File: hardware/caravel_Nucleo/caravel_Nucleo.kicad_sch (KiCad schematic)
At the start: 6 parts, among them J10 Conn_01x09_Female, J3 Conn_01x02_Male, J5 Conn_01x02_Male, T1 Logo, T2 Logo, U11 NUCLEO144-F429ZI

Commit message: [in review] update caravel board Nucleo-144 hat
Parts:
- added C1: 0.01uf - CC0805JRX7R9BB103, Capacitor_SMD:C_0805_2012Metric, symbol Device:C
- added C10, C13, C18, C20, C21: 1uf - CC0805KKX5R8BB105, Capacitor_SMD:C_0805_2012Metric, symbol Device:C
- added C11, C14, C19: 0.01uf - CC0805KRX7R9BB103, Capacitor_SMD:C_0805_2012Metric, symbol Device:C
- added C12, C15: 10uf - CC0805KKX5R8BB106, Capacitor_SMD:C_0805_2012Metric, symbol Device:C
- added C16, C17, C2, C3, C4, C5, C6, C7, C8, C9: 0.1uf - CC0805KRX7R9BB104, Capacitor_SMD:C_0805_2012Metric, symbol Device:C
- added D1, D2, D3, D4: LED - 17-215SURC/S530-A2/TR8, LED_SMD:LED_1206_3216Metric, symbol Device:LED
- added J1: USB_B_Micro - 10118193-0001LF, strive_foot_prints:FCI_10118193-0001LF, symbol Connector:USB_B_Micro
- added J11, J8, J9: Conn_01x03, Connector_PinHeader_2.54mm:PinHeader_1x03_P2.54mm_Vertical, symbol Connector_Generic:Conn_01x03
- added J2: Conn_01x02_Female, Connector_PinHeader_2.54mm:PinHeader_1x02_P2.54mm_Vertical, symbol Connector:Conn_01x02_Female
- added J4: Conn_01x04_Female, Connector_PinHeader_2.54mm:PinHeader_1x04_P2.54mm_Vertical, symbol Connector:Conn_01x04_Female
- added J6: Conn_01x02_Male, Connector_PinHeader_2.54mm:PinHeader_1x02_P2.54mm_Vertical, symbol Connector:Conn_01x02_Male
- added J7: Conn_01x06_Female, Connector_PinHeader_2.54mm:PinHeader_1x06_P2.54mm_Vertical, symbol Connector:Conn_01x06_Female
- added R1, R10, R11, R12, R7, R8, R9: 10k - RC0805FR-0710KL, Resistor_SMD:R_0805_2012Metric, symbol Device:R
- added R13, R14: 82 - 0805W8F820JT5E, Resistor_SMD:R_0805_2012Metric, symbol Device:R
- added R15, R16, R17, R18, R27, R5, R6: 10k, Resistor_SMD:R_0805_2012Metric, symbol Device:R
- added R19: 360 1% - 0805W8F1202T5E, Resistor_SMD:R_0805_2012Metric, symbol Device:R
- added R2: 12K 1% - 0805W8F1202T5E, Resistor_SMD:R_0805_2012Metric, symbol Device:R
- added R20, R23: 4.99K 1% - 0805W8F1202T5E, Resistor_SMD:R_0805_2012Metric, symbol Device:R
- added R21: 499 1% - 0805W8F1202T5E, Resistor_SMD:R_0805_2012Metric, symbol Device:R
- added R22: 4.22K 1% - 0805W8F1202T5E, Resistor_SMD:R_0805_2012Metric, symbol Device:R
- added R24: 4.02K 1% - 0805W8F1202T5E, Resistor_SMD:R_0805_2012Metric, symbol Device:R
- added R25, R26: 4.7K 1% - 0805W8F1202T5E, Resistor_SMD:R_0805_2012Metric, symbol Device:R
- added R3, R4: 150 - 0805W8J0151T5E, Resistor_SMD:R_0805_2012Metric, symbol Device:R
- added SW1: SW_Push - SKQGADE010, strive_foot_prints:SW4-SMD-5.2X5.2X1.5MM, symbol Switch:SW_Push
- added TP1, TP2: TestPoint, TestPoint:TestPoint_Bridge_Pitch2.54mm_Drill1.0mm, symbol Connector:TestPoint
- added U1: FT232H, Package_DFN_QFN:QFN-48-1EP_8x8mm_P0.5mm_EP6.2x6.2mm, symbol Interface_USB:FT232H
- added U10: MCP4661, Caravel_Board:QFN-16-1EP_4x4mm_P0.65mm_EP2.5x2.5mm, symbol Caravel_board:MCP4661
- added U2, U3: SN74LVC1G125DCKR, SOT65P210X110-5N, symbol Caravel_board:SN74LVC1G125DCKR
- added U4: MCP1319MT-29LE-OT, Caravel_Board:PoR_5_SOT23, symbol Caravel_board:MCP1319MT-29LE-OT
- added U5, U6: TAR5SxxU_SOT353F, Caravel_Board:SOT-353F, symbol Caravel_board:TAR5SxxU_SOT353F
- added U7: W25Q32FVSS, strive_foot_prints:SOIC127P790X216-8N, symbol Caravel_board:W25Q32FVSS
- added U8: caravel_breakout, Caravel_Board:caravel_breakout_flexy, symbol Caravel_board:caravel_breakout_v2
- added U9: MIC2211-AAYML-TR, Caravel_Board:10-pin_MLF_P0.5, symbol Caravel_board:MIC2211-AAYML-TR
- added X1: DSC6001_10MHZ, strive_foot_prints:DSC6001JE1A-010.0000, symbol Oscillator:XO91
- added Y1: CSTNE12M0GH5L000R0, strive_foot_prints:CSTNE12M0GH5L000R0, symbol Device:Crystal_GND2
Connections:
- net vccd1 is gone; now on net +1V8: J3.2 (Pin_2)
- net vddio is gone; now on net +3V3: J5.2 (Pin_2)
- net +1V8: now also J8.2 (Pin_2), U8.43 (vccd1), U8.50 (vccd), U8.6 (vccd)
- net +3V3: now also C16.2, C17.1, C4.2, C5.2, C6.2, C7.2, C8.2, C9.2, J4.4 (Pin_4), J9.2 (Pin_2), R1.2, R10.2, R11.2, R12.2, R13.1, R14.1, R3.2, R4.2, R5.1, R6.1, R7.2, R8.2, R9.2, U1.12 (VCCIO), U1.24 (VCCIO), U1.3 (VPHY), U1.39 (VCCD), U1.40 (VREGIN), U1.46 (VCCIO), U1.8 (VPLL), U2.5 (VCC), U3.5 (VCC), U4.5 (VDD), U7.8 (VCC), U8.45 (vdda), U8.55 (vddio), U8.7 (vddio), X1.4 (V+)
- net +5V: now also C10.2, C13.2, C18.2, J1.1 (VBUS), R15.2, R16.2, R17.2, R18.2, R25.1, R26.1, R27.2, U10.14 (VDD), U5.5 (VIN), U6.5 (VIN), U9.1 (VIN)
- net Caravel_CSB: now also J7.1 (Pin_1), R7.1, U7.1 (~{CS}), U8.51 (Caravel_CSB)
- net Caravel_D0: now also J7.4 (Pin_4), R10.1, U7.5 (SI(D0)), U8.49 (Caravel_D0)
- net Caravel_D1: now also J7.2 (Pin_2), R8.1, U7.2 (SO(D1)), U8.48 (Caravel_D1)
- net Caravel_SCK: now also J7.5 (Pin_5), R11.1, U7.6 (SCK), U8.46 (Caravel_SCK)
- net GND: now also C1.1, C10.1, C11.2, C12.1, C13.1, C14.2, C15.1, C16.1, C17.2, C18.1, C19.2, C2.1, C20.2, C21.2, C3.1, C4.1, C5.1, C6.1, C7.1, C8.1, C9.1, D4.1 (K), J1.5 (GND), J2.1 (Pin_1), J4.1 (Pin_1), J6.2 (Pin_2), R2.1, R20.1, R24.1, SW1.2, TP1.1, TP2.1, U1.10 (GND), U1.11 (GND), U1.22 (GND), U1.23 (GND), U1.35 (GND), U1.36 (GND), U1.4 (AGND), U1.41 (AGND), U1.42 (TEST), U1.47 (GND), U1.48 (GND), U1.9 (AGND), U10.1 (HVC/A0), U10.10 (P0B), U10.12 (A2), U10.13 (A1), U10.4 (VSS), U10.5 (P1B), U2.3 (GND), U3.3 (GND), U4.2 (VSS), U5.2 (GND), U6.2 (GND), U7.4 (GND), U8.5 (GND), U8.8 (GND), U9.6 (GND), X1.2 (GND), Y1.2
- net I2C2_SCL: now also R25.2, U10.2 (SCL)
- net I2C2_SDA: now also R26.2, U10.3 (SDA)
- net SPI5_CS: now also U1.16 (ADBUS3), U8.39 (mprj_io[3]_CSB)
- net SPI5_MISO: now also U1.14 (ADBUS1), U2.4 (Y), U8.40 (mprj_io[2]_SDI)
- net SPI5_MOSI: now also U1.15 (ADBUS2), U8.41 (mprj_io[1]_SDO)
- net SPI5_SCK: now also U1.13 (ADBUS0), U3.2 (A), U8.38 (mprj_io[4]_SCK)
- net TIM3_CH2: now also J11.1 (Pin_1); no longer J10.9 (Pin_9)
- net gpio: now also D3.1 (K), U8.47 (gpio)
- net mprj_io[0]: now also U8.42 (mprj_io[0])
- net mprj_io[10]: now also U8.32 (mprj_io[10])
- net mprj_io[11]: now also U8.31 (mprj_io[11])
- net mprj_io[12]: now also U8.30 (mprj_io[12])
- net mprj_io[13]: now also U8.29 (mprj_io[13])
- net mprj_io[14]: now also U8.28 (mprj_io[14])
- net mprj_io[15]: now also U8.27 (mprj_io[15])
- net mprj_io[16]: now also U8.26 (mprj_io[16])
- net mprj_io[17]: now also U8.25 (mprj_io[17])
- net mprj_io[18]: now also U8.24 (mprj_io[18])
- net mprj_io[19]: now also U8.23 (mprj_io[19])
- net mprj_io[20]: now also U8.22 (mprj_io[20])
- net mprj_io[21]: now also U8.21 (mprj_io[21])
- net mprj_io[22]: now also U8.20 (mprj_io[22])
- net mprj_io[23]: now also U8.19 (mprj_io[23])
- net mprj_io[24]: now also U8.18 (mprj_io[24])
- net mprj_io[25]: now also U8.17 (mprj_io[25])
- net mprj_io[26]: now also U8.16 (mprj_io[26])
- net mprj_io[27]: now also U8.15 (mprj_io[27])
- net mprj_io[28]: now also U8.14 (mprj_io[28])
- net mprj_io[29]: now also U8.13 (mprj_io[29])
- net mprj_io[30]: now also U8.12 (mprj_io[30])
- net mprj_io[31]: now also U8.11 (mprj_io[31])
- net mprj_io[32]: now also U8.10 (mprj_io[32])
- net mprj_io[33]: now also U8.9 (mprj_io[33])
- net mprj_io[34]: now also U8.4 (mprj_io[34])
- net mprj_io[35]: now also U8.3 (mprj_io[35])
- net mprj_io[36]: now also U8.2 (mprj_io[36])
- net mprj_io[37]: now also U8.1 (mprj_io[37])
- net mprj_io[7]: now also U8.35 (mprj_io[7])
- net mprj_io[8]: now also U8.34 (mprj_io[8])
- net mprj_io[9]: now also U8.33 (mprj_io[9])
- net vccd2: now also U8.56 (vccd2)
- net vdda1: now also U8.44 (vdda1)
- net vdda2: now also U8.54 (vdda2)
- net ~{RST}: now also U4.1 (~{RST}), U8.53 (~{RST})
- net UART8_RX: now reaches U11.136 (PE0)
- net UART8_RX: now also J4.3 (Pin_3), U2.2 (A), U8.36 (mprj_io[6]_ser_tx)
- net PH0: now reaches U11.29 (PH0)
- net PH0: now also J11.3 (Pin_3)
- net UART8_TX: now reaches U11.61 (PE1)
- net UART8_TX: now also J4.2 (Pin_2), U3.4 (Y), U8.37 (mprj_io[5]_ser_rx)
- net UART3_RX: no longer names the net of U11.2 (PC11)
- net UART3_TX: no longer names the net of U11.1 (PC10)
- new net: R2.2, U1.5 (REF)
- new net: R16.1, U6.1 (Control)
- new net: C14.1, U6.3 (Noise)
- new net: R27.1, U10.11 (~{WP})
- new net: R23.1, U10.6 (P1W)
- new net: R21.1, U10.9 (P0W)
- new net: J6.1 (Pin_1), X1.1 (EN)
- new net: R18.1, U9.2 (EN1)
- new net: C11.1, U5.3 (Noise)
- new net: R19.1, R20.2, R21.2, U9.5 (ADJ1)
- new net: D4.2 (A), R14.2
- new net: C19.1, U9.4 (BYP)
- new net: R22.1, R23.2, R24.2, U9.7 (ADJ2)
- new net: U1.1 (XCSI), Y1.1
- new net: U1.2 (XCSO), Y1.3
- new net: D2.1 (K), U1.26 (ACBUS2)
- new net: D1.1 (K), U1.27 (ACBUS3)
- new net: C1.2, R1.1, U1.34 (~{RESET})
- new net: C3.2, U1.37 (VCCA)
- new net: C2.2, U1.38 (VCCCORE)
- new net: D2.2 (A), R4.1
- new net: D3.2 (A), R13.2
- new net: D1.2 (A), R3.1
- new net: R15.1, U5.1 (Control)
- new net: R17.1, U9.3 (EN2)
- new net FTDI_D+: J1.3 (D+), U1.7 (DP)
- new net FTDI_D-: J1.2 (D-), U1.6 (DM)
- new net UART_EN: J2.2 (Pin_2), R5.2, R6.2, U1.21 (ACBUS0), U2.1 (~{OE}), U3.1 (~{OE})
- new net V1.8: C15.2, J8.1 (Pin_1), U6.4 (VOUT)
- new net V3.3: C12.2, J9.1 (Pin_1), U5.4 (VOUT)
- new net VOUT1: C20.1, J9.3 (Pin_3), R19.2, U9.10 (VOUT1)
- new net VOUT2: C21.1, J8.3 (Pin_3), R22.2, U9.9 (VOUT2)
- new net xclk: J10.9 (Pin_9), J11.2 (Pin_2), U8.52 (xclk), X1.3 (OUT)
- new net ~{MEM_HOLD}: J7.6 (Pin_6), R12.1, U7.7 (~{HOLD}(D3))
- new net ~{MEM_WP}: J7.3 (Pin_3), R9.1, U7.3 (~{WP}(D2))
- new net ~{MR}: SW1.1, U4.4 (~{MR})
- no-connect marks 7 -> 24
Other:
- removed sheet Caravel Board
- note added: "Buffers to enable FTDI UART interface"
- note added: "Dynamic Power Supplies"
- note added: "FTDI Module"
- note added: "FTDI interface with HKSPI"
- note added: "Flash memory"
- note added: "Flash memory interface with Caravel"
- note added: "LEDs"
- note added: "MEMS Oscillator"
- note added: "Memory testing"
- note added: "Power on Reset"
- note added: "Serial Display"
- note added: "USB Module"
- note added: "Voltage Regulator"
- moved on the sheet: J10, J3, J5, U11

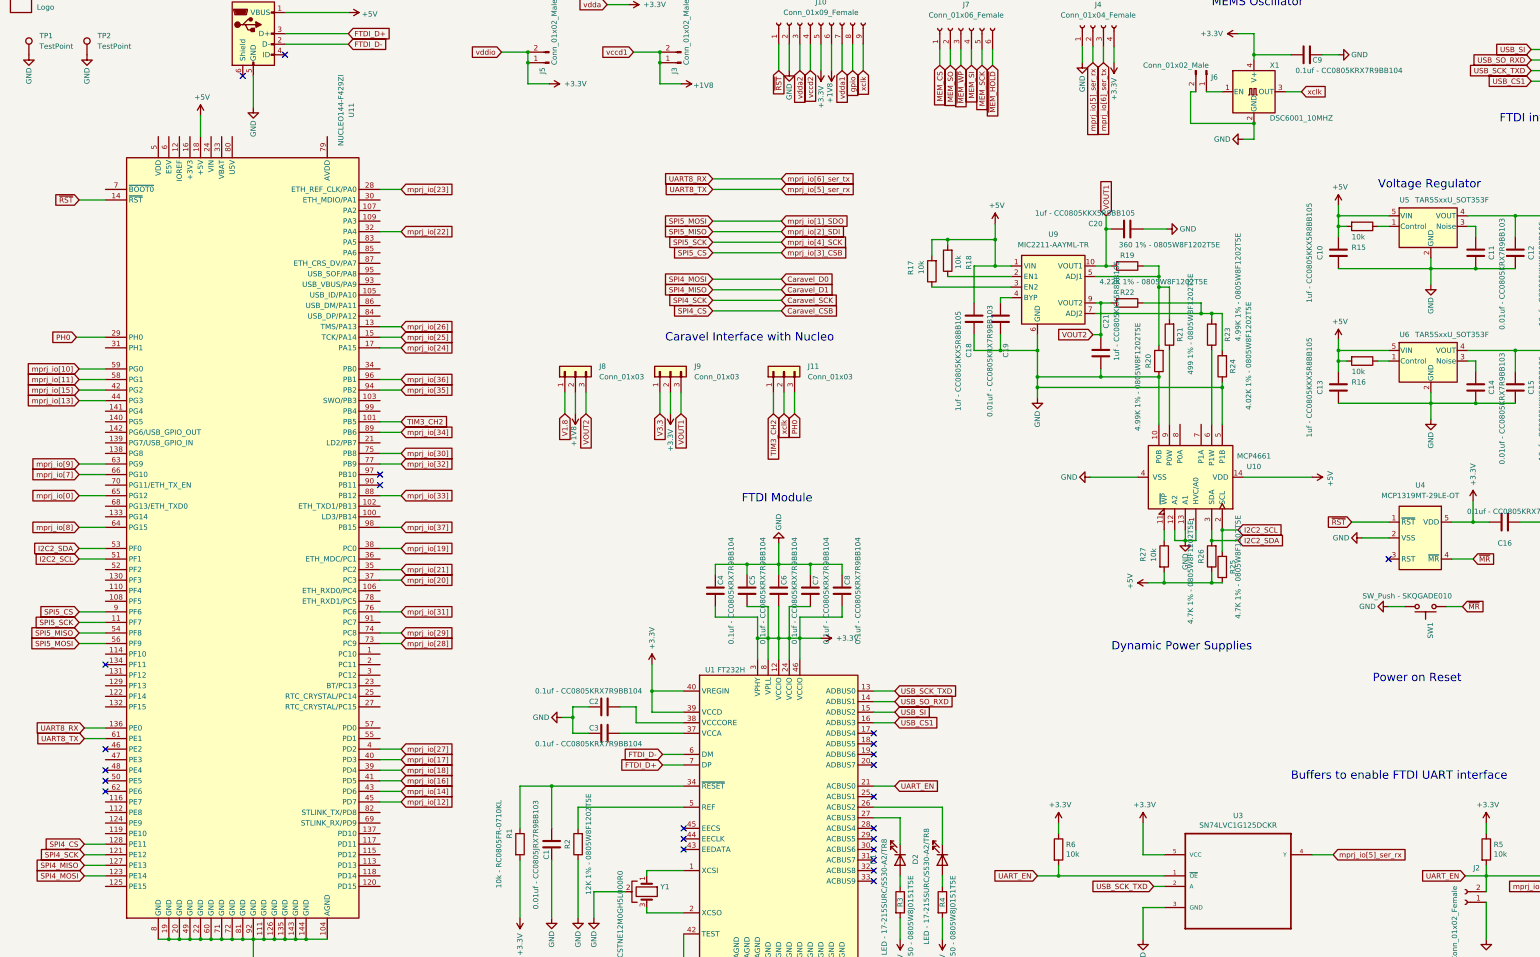
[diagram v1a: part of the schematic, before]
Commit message: update caravel board Nucleo-144 hat
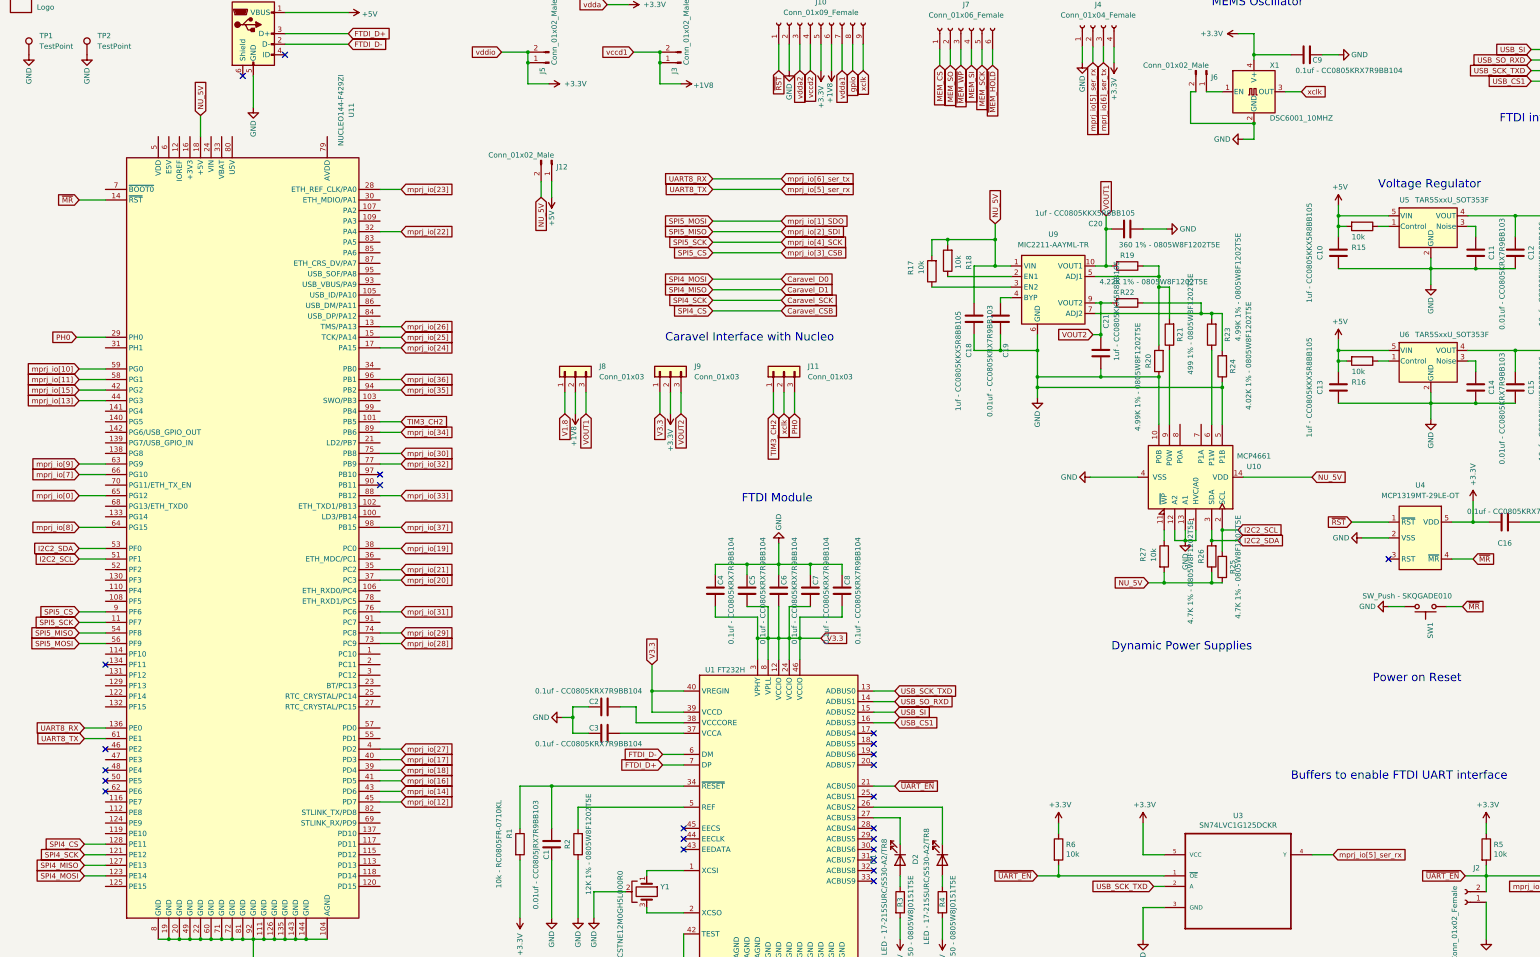
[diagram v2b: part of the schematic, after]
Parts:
- added J12: Conn_01x02_Male, Connector_PinHeader_2.54mm:PinHeader_1x02_P2.54mm_Vertical, symbol Connector:Conn_01x02_Male
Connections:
- net +3V3: no longer C4.2, C5.2, C6.2, C7.2, C8.2, U1.12 (VCCIO), U1.24 (VCCIO), U1.3 (VPHY), U1.39 (VCCD), U1.40 (VREGIN), U1.46 (VCCIO), U1.8 (VPLL)
- net +5V: now also J12.1 (Pin_1); no longer C18.2, R17.2, R18.2, R25.1, R26.1, R27.2, U10.14 (VDD), U11.18 (+5V), U9.1 (VIN)
- net V3.3: now also C4.2, C5.2, C6.2, C7.2, C8.2, U1.12 (VCCIO), U1.24 (VCCIO), U1.3 (VPHY), U1.39 (VCCD), U1.40 (VREGIN), U1.46 (VCCIO), U1.8 (VPLL)
- net VOUT1: now also J8.3 (Pin_3); no longer J9.3 (Pin_3)
- net VOUT2: now also J9.3 (Pin_3); no longer J8.3 (Pin_3)
- net ~{MR}: now also U11.14 (~{RST})
- net ~{RST}: no longer U11.14 (~{RST})
- net UART_EN renamed ~{UART_EN}
- new net NU_5V: C18.2, J12.2 (Pin_2), R17.2, R18.2, R25.1, R26.1, R27.2, U10.14 (VDD), U11.18 (+5V), U9.1 (VIN)

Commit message: update caravel nucleo hat board Rev A
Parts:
- removed TP2: TestPoint, TestPoint:TestPoint_Bridge_Pitch2.54mm_Drill1.0mm, symbol Connector:TestPoint
- added C22: 1uf - CC0805KKX5R8BB105, Capacitor_SMD:C_0805_2012Metric, symbol Device:C
- added C23: 0.01uf - CC0805KRX7R9BB103, Capacitor_SMD:C_0805_2012Metric, symbol Device:C
- added C24: 10uf - CC0805KKX5R8BB106, Capacitor_SMD:C_0805_2012Metric, symbol Device:C
- added R28: 10k, Resistor_SMD:R_0805_2012Metric, symbol Device:R
- added R29, R30, R31, R32: 0, Resistor_SMD:R_0805_2012Metric, symbol Device:R
- added U11: TAR5SxxU_SOT353F, Caravel_Board:SOT-353F, symbol Caravel_board:TAR5SxxU_SOT353F
- J10: value Conn_01x09_Female -> Conn_01x11_Female; footprint Connector_PinHeader_2.54mm:PinHeader_1x09_P2.54mm_Vertical -> Connector_PinHeader_2.54mm:PinHeader_1x11_P2.54mm_Vertical; symbol Connector:Conn_01x09_Female -> Connector:Conn_01x11_Female
- U9: footprint Caravel_Board:10-pin_MLF_P0.5 -> Package_DFN_QFN:DFN-10-1EP_3x3mm_P0.5mm_EP1.65x2.38mm
- renumbered U11 to U12
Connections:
- net +1V8: now also J10.3 (Pin_3), J10.4 (Pin_4), J10.5 (Pin_5); no longer J10.6 (Pin_6)
- net +3V3: now also J10.7 (Pin_7), J10.8 (Pin_8); no longer J10.5 (Pin_5), R1.2, R3.2, R4.2
- net +5V: now also C22.2, R28.2, U11.5 (VIN)
- net Caravel_CSB: now also R32.1; no longer U12.128 (PE11)
- net Caravel_D0: now also R29.1; no longer U12.123 (PE14)
- net Caravel_D1: now also R30.1; no longer U12.127 (PE13)
- net Caravel_SCK: now also R31.1; no longer U12.121 (PE12)
- net GND: now also C22.1, C23.2, C24.1, U11.2 (GND); no longer J10.2 (Pin_2)
- net V3.3: no longer C4.2, C5.2, C6.2, C7.2, C8.2, U1.12 (VCCIO), U1.24 (VCCIO), U1.3 (VPHY), U1.39 (VCCD), U1.40 (VREGIN), U1.46 (VCCIO), U1.8 (VPLL)
- net gpio: now also J10.10 (Pin_10); no longer J10.8 (Pin_8)
- net vccd2: now also J10.2 (Pin_2); no longer J10.4 (Pin_4)
- net vdda1: now also J10.9 (Pin_9); no longer J10.7 (Pin_7)
- net vdda2: now also J10.6 (Pin_6); no longer J10.3 (Pin_3)
- net xclk: now also J10.11 (Pin_11); no longer J10.9 (Pin_9)
- net ~{MR}: now also U1.25 (ACBUS1), U12.3 (PC12); no longer U12.14 (~{RST})
- net EN_V1.8: now reaches R16.1, U6.1 (Control)
- net EN_V1.8: now also U1.29 (ACBUS5)
- net EN_VOUT1: now reaches R18.1, U9.2 (EN1)
- net EN_VOUT1: now also U12.21 (LD2/PB7)
- net EN_V3.3: now reaches U1.30 (ACBUS6)
- net EN_V3.3: now also R15.1, U5.1 (Control)
- net EN_VOUT2: now reaches U12.23 (BT/PC13)
- net EN_VOUT2: now also R17.1, U9.3 (EN2)
- new net: R28.1, U11.1 (Control)
- new net: C23.1, U11.3 (Noise)
- new net FTDI_V3.3: C24.2, C4.2, C5.2, C6.2, C7.2, C8.2, R1.2, R3.2, R4.2, U1.12 (VCCIO), U1.24 (VCCIO), U1.3 (VPHY), U1.39 (VCCD), U1.40 (VREGIN), U1.46 (VCCIO), U1.8 (VPLL), U11.4 (VOUT)
- new net SPI4_CS: R32.2, U12.128 (PE11)
- new net SPI4_MISO: R30.2, U12.127 (PE13)
- new net SPI4_MOSI: R29.2, U12.123 (PE14)
- new net SPI4_SCK: R31.2, U12.121 (PE12)
- no-connect marks 24 -> 20
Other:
- note added: "FTDI Voltage Regulator"
- note added: "Optional Nucleo Interface with FLASH"
- moved on the sheet: C13, C17, D1, D2, D3, D4, J11, J2, J8, J9, R10, R11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
